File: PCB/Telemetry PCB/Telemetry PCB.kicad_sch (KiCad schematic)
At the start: 47 parts, among them IC1 E22-900M22S, J1 Conn_01x04_Pin, J2 Serial Debug Header 1x4, J3 GPS, J4 Batt, J5 USB_C_Receptacle_USB2.0_16P, SW1 SW_MEC_5E, SW2 SW_MEC_5E, U1 STM32F411CEUx, U2 MCP1700x-250xxTT, U3 AP62200WU, Y1 25MHZ 20pF, Y2 32.768k 12.5pF

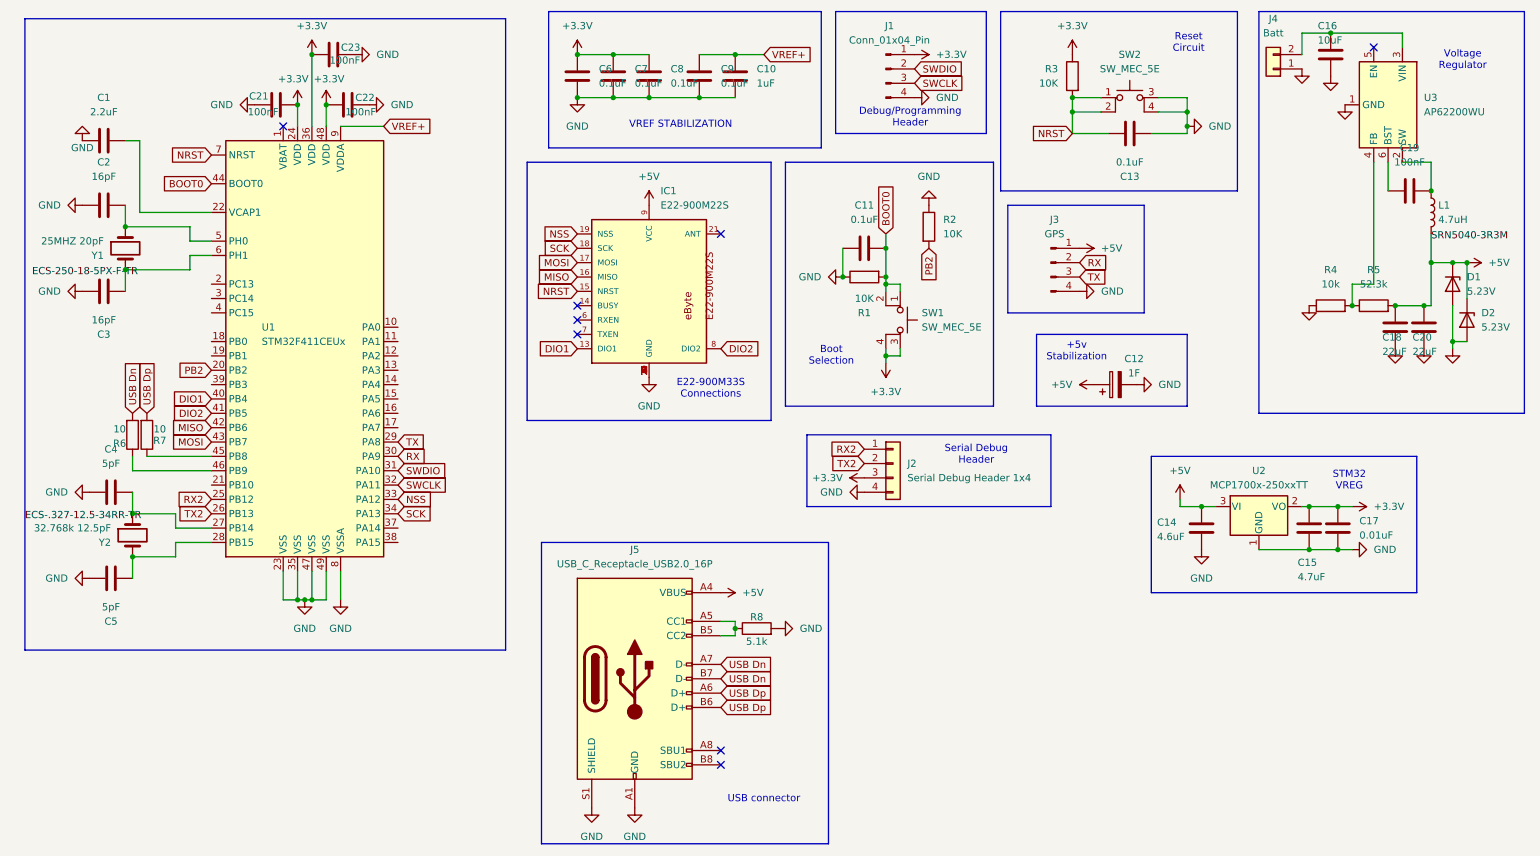
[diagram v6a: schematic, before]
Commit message: reannotated based on board geometry
reannotated based on board geometry
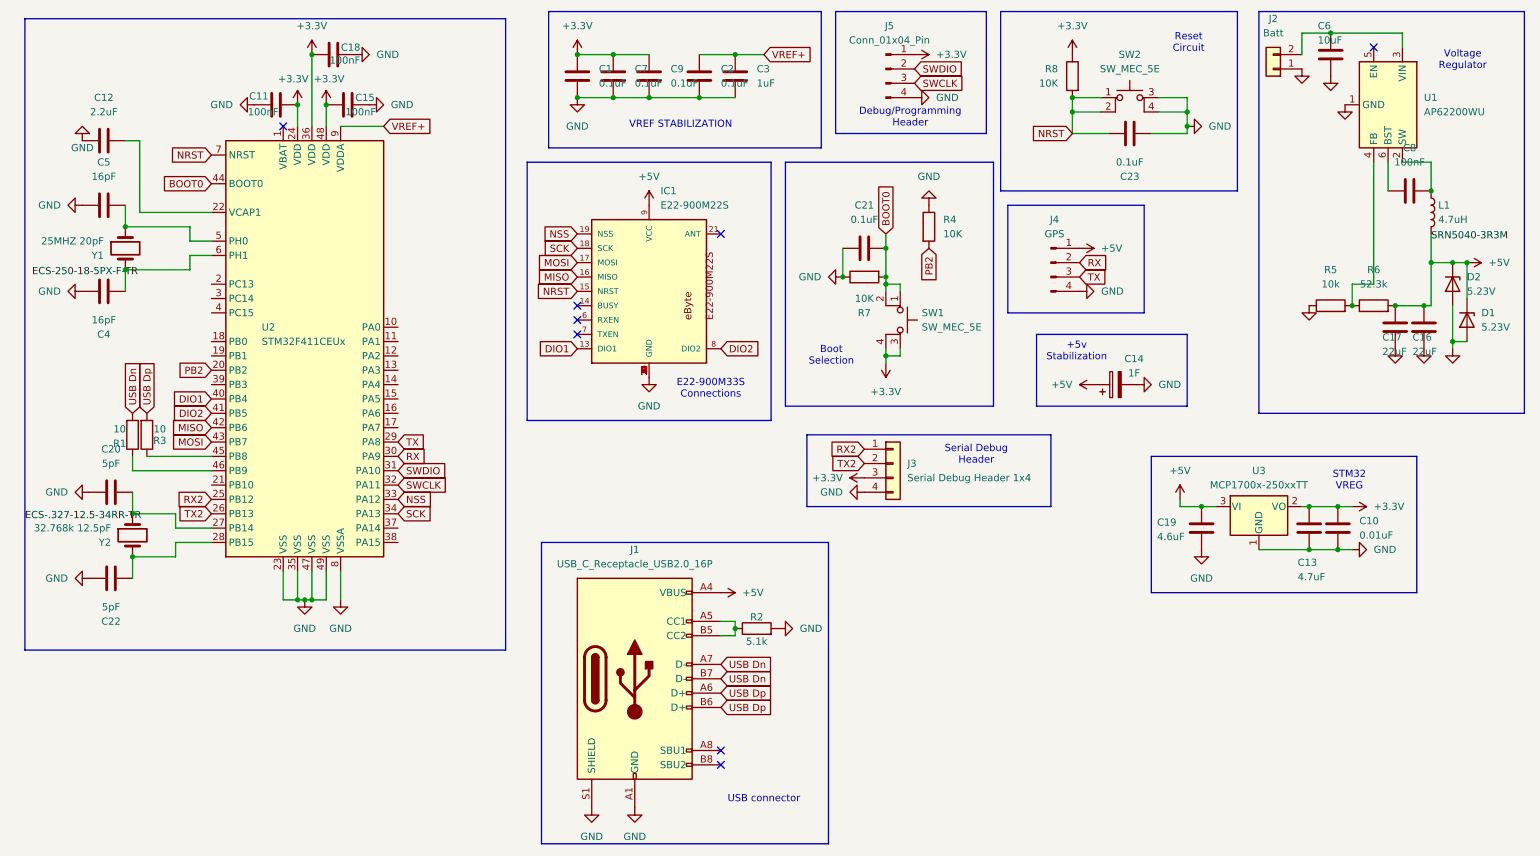
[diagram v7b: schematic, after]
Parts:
- renumbered C6 to C1, C17 to C10, C21 to C11, C1 to C12, C15 to C13, C12 to C14, C22 to C15, C20 to C16, C18 to C17, C23 to C18, C14 to C19, C9 to C2, C4 to C20, C11 to C21, C5 to C22, C13 to C23, C10 to C3, C3 to C4, C2 to C5, C16 to C6, C19 to C8, C8 to C9, D2 to D1, D1 to D2, J5 to J1, J4 to J2, J2 to J3, J3 to J4, J1 to J5, R6 to R1, R8 to R2, R7 to R3, R2 to R4, R4 to R5, R5 to R6, R1 to R7, R3 to R8, U3 to U1, U1 to U2, U2 to U3

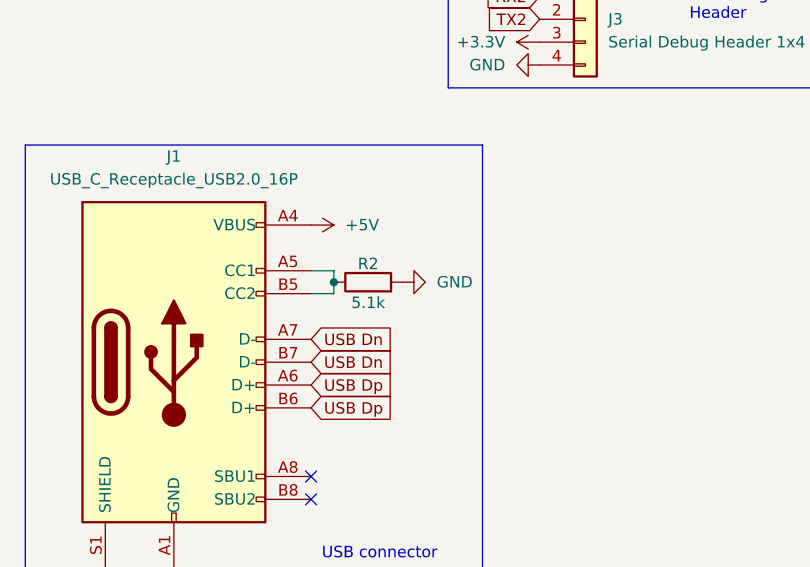
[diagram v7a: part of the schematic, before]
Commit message: Tweaked usb and data traces
Tweaked usb board should be able to be powered by usb without catching fire

I also moved some data traces away from each other and filled between them to lower their parasitic capacitance
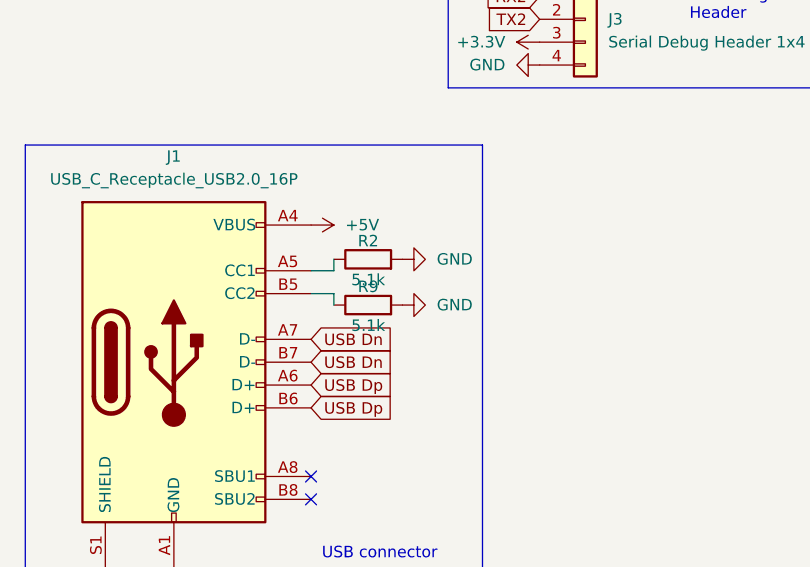
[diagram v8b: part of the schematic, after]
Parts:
- added R9: 5.1k, Capacitor_SMD:C_1206_3216Metric_Pad1.33x1.80mm_HandSolder, symbol Device:R
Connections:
- net GND: now also R9.2
- net at J1.A5 (CC1), R2.1: no longer J1.B5 (CC2)
- new net: J1.B5 (CC2), R9.1
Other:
- moved on the sheet: R2
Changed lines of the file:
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@@
 	)
 	(junction
-		(at 142.24 124.46)
-		(diameter 0)
-		(color 0 0 0 0)
-	)
-	(junction
 		(at 168.91 62.23)
 		(diameter 0)
@@
 	(wire
 		(pts
-			(xy 142.24 124.46) (xy 142.24 123.19)
-		)
-		(stroke
-			(width 0)
-			(type default)
-		)
-	)
-	(wire
-		(pts
 			(xy 114.3 22.86) (xy 120.65 22.86)
 		)
@@
 	(wire
 		(pts
-			(xy 142.24 125.73) (xy 142.24 124.46)
-		)
-		(stroke
-			(width 0)
-			(type default)
-		)
-	)
-	(wire
-		(pts
 			(xy 265.43 54.61) (xy 265.43 59.69)
 		)
@@
 	(wire
 		(pts
+			(xy 142.24 121.92) (xy 142.24 123.19)
+		)
+		(stroke
+			(width 0)
+			(type default)
+		)
+	)
+	(wire
+		(pts
 			(xy 43.18 111.76) (xy 35.56 111.76)
 		)
@@
 	(wire
 		(pts
+			(xy 142.24 125.73) (xy 142.24 127)
+		)
+		(stroke
+			(width 0)
+			(type default)
+		)
+	)
+	(wire
+		(pts
 			(xy 49.53 109.22) (xy 43.18 109.22)
 		)
@@
 		(lib_name "GND_16")
 		(lib_id "power:GND")
-		(at 149.86 124.46 90)
+		(at 149.86 121.92 90)
 		(unit 1)
 		(exclude_from_sim no)
@@
 		(fields_autoplaced yes)
 		(property "Reference" "#PWR041"
-			(at 156.21 124.46 0)
+			(at 156.21 121.92 0)
 			(effects
 				(font
@@
 		)
 		(property "Value" "GND"
-			(at 153.67 124.4599 90)
+			(at 153.67 121.9199 90)
 			(effects
 				(font
@@
 		)
 		(property "Footprint" ""
-			(at 149.86 124.46 0)
+			(at 149.86 121.92 0)
 			(effects
 				(font
@@
 		)
 		(property "Datasheet" ""
-			(at 149.86 124.46 0)
+			(at 149.86 121.92 0)
 			(effects
 				(font
@@
 		)
 		(property "Description" "Power symbol creates a global label with name \"GND\" , ground"
-			(at 149.86 124.46 0)
+			(at 149.86 121.92 0)
 			(effects
 				(font
@@
 	)
 	(symbol
+		(lib_id "Device:R")
+		(at 146.05 127 90)
+		(unit 1)
+		(exclude_from_sim no)
+		(in_bom yes)
+		(on_board yes)
+		(dnp no)
+		(property "Reference" "R9"
+			(at 146.05 124.968 90)
+			(effects
+				(font
+					(size 1.27 1.27)
+				)
+			)
+		)
+		(property "Value" "5.1k"
+			(at 146.05 129.286 90)
+			(effects
+				(font
+					(size 1.27 1.27)
+				)
+			)
+		)
+		(property "Footprint" "Capacitor_SMD:C_1206_3216Metric_Pad1.33x1.80mm_HandSolder"
+			(at 146.05 128.778 90)
+			(effects
+				(font
+					(size 1.27 1.27)
+				)
+				(hide yes)
+			)
+		)
+		(property "Datasheet" "~"
+			(at 146.05 127 0)
+			(effects
+				(font
+					(size 1.27 1.27)
+				)
+				(hide yes)
+			)
+		)
+		(property "Description" "Resistor"
+			(at 146.05 127 0)
+			(effects
+				(font
+					(size 1.27 1.27)
+				)
+				(hide yes)
+			)
+		)
+		(pin "2"
+		)
+		(pin "1"
+		)
+		(instances
+			(project "Telemetry PCB"
+				(path "/d3e58202-7594-4bd8-a3d4-cb0300333d9c"
+					(reference "R9")
+					(unit 1)
+				)
+			)
+		)
+	)
+	(symbol
 		(lib_name "+3.3V_5")
 		(lib_id "power:+3.3V")
@@
 	(symbol
 		(lib_id "Device:R")
-		(at 146.05 124.46 90)
+		(at 146.05 121.92 90)
 		(unit 1)
 		(exclude_from_sim no)
@@
 		(dnp no)
 		(property "Reference" "R2"
-			(at 146.05 122.428 90)
+			(at 146.05 119.888 90)
 			(effects
 				(font
@@
 		)
 		(property "Value" "5.1k"
-			(at 146.05 126.746 90)
+			(at 146.05 124.206 90)
 			(effects
 				(font
@@
 		)
 		(property "Footprint" "Capacitor_SMD:C_1206_3216Metric_Pad1.33x1.80mm_HandSolder"
-			(at 146.05 126.238 90)
+			(at 146.05 123.698 90)
 			(effects
 				(font
@@
 		)
 		(property "Datasheet" "~"
-			(at 146.05 124.46 0)
+			(at 146.05 121.92 0)
 			(effects
 				(font
@@
 		)
 		(property "Description" "Resistor"
-			(at 146.05 124.46 0)
+			(at 146.05 121.92 0)
 			(effects
 				(font
@@
 					(unit 1)
 				)
+			)
+		)
+	)
+	(symbol
+		(lib_name "GND_16")
+		(lib_id "power:GND")
+		(at 149.86 127 90)
+		(unit 1)
+		(exclude_from_sim no)
+		(in_bom yes)
+		(on_board yes)
+		(dnp no)
+		(fields_autoplaced yes)
+		(property "Reference" "#PWR047"
+			(at 156.21 127 0)
+			(effects
+				(font
+					(size 1.27 1.27)
+				)
+				(hide yes)
+			)
+		)
+		(property "Value" "GND"
+			(at 153.67 126.9999 90)
+			(effects
+				(font
+					(size 1.27 1.27)
+				)
+				(justify right)
+			)
+		)
+		(property "Footprint" ""
+			(at 149.86 127 0)
+			(effects
+				(font
+					(size 1.27 1.27)
+				)
+				(hide yes)
+			)
+		)
+		(property "Datasheet" ""
+			(at 149.86 127 0)
+			(effects
+				(font
+					(size 1.27 1.27)
+				)
+				(hide yes)
+			)
+		)
+		(property "Description" "Power symbol creates a global label with name \"GND\" , ground"
+			(at 149.86 127 0)
+			(effects
+				(font
+					(size 1.27 1.27)
+				)
+				(hide yes)
+			)
+		)
+		(pin "1"
+		)
+		(instances
+			(project "Telemetry PCB"
+				(path "/d3e58202-7594-4bd8-a3d4-cb0300333d9c"
+					(reference "#PWR047")
+					(unit 1)
+				)
